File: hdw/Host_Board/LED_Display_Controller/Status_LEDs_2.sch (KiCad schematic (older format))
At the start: 16 parts

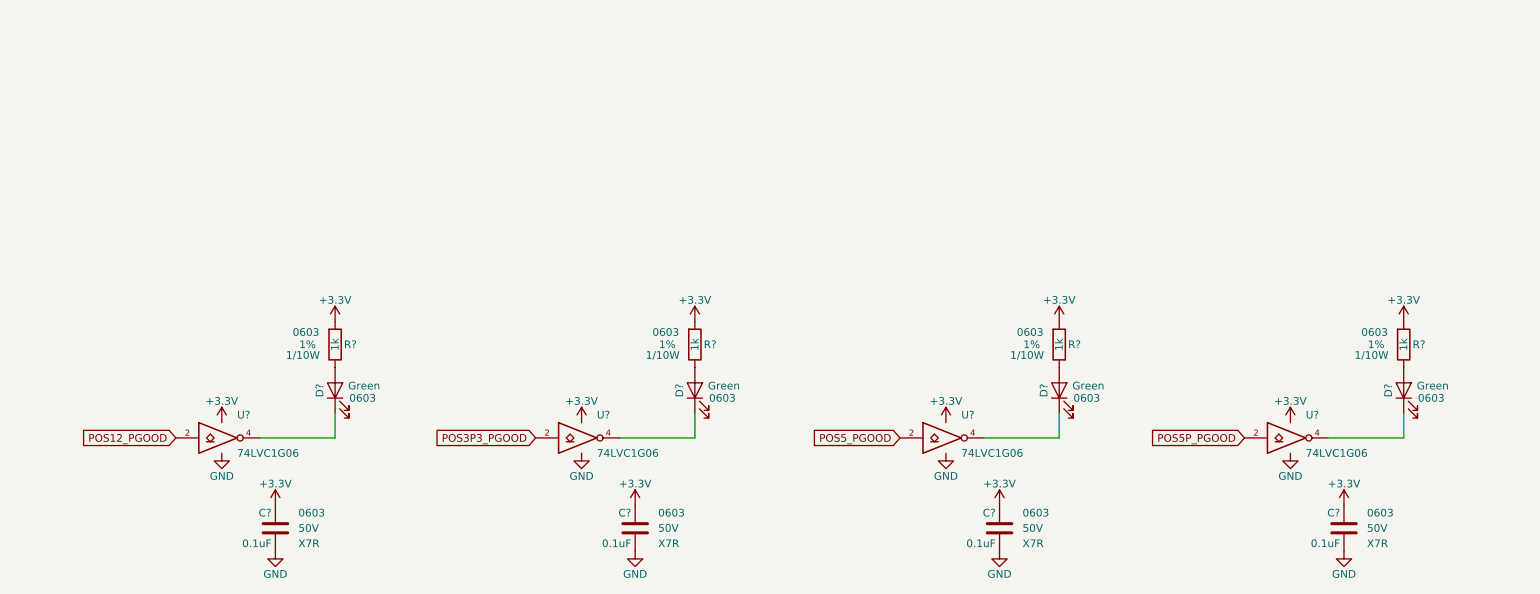
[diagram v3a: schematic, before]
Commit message: Added titles and MU logo to each sheet
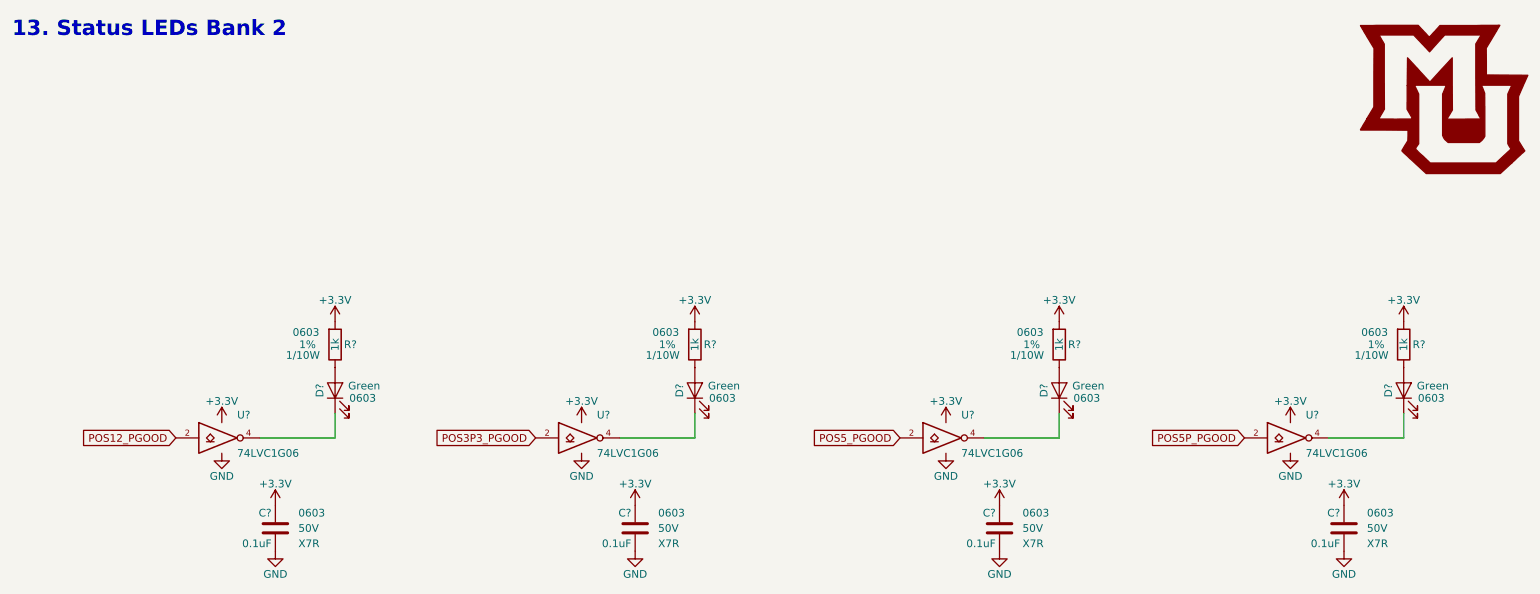
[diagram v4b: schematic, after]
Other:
- note added: "13. Status LEDs Bank 2"
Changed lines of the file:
@@
 AR Path="/5BB844FD/5BF380D7" Ref="#PWR?"  Part="1"
 AR Path="/5BF346B3/5BF380D7" Ref="#PWR0546"  Part="1"
-F 0 "#PWR?" H 2660 2400 50  0001 C CNN
+F 0 "#PWR0546" H 2660 2400 50  0001 C CNN
 F 1 "+3.3V" H 2660 2690 50  0000 C CNN
 F 2 "" H 2660 2550 50  0001 C CNN
@@
 AR Path="/5BB844FD/5BF380E5" Ref="#PWR?"  Part="1"
 AR Path="/5BF346B3/5BF380E5" Ref="#PWR0547"  Part="1"
-F 0 "#PWR?" H 1920 3160 50  0001 C CNN
+F 0 "#PWR0547" H 1920 3160 50  0001 C CNN
 F 1 "GND" H 1920 3260 50  0000 C CNN
 F 2 "" H 1920 3410 50  0001 C CNN
@@
 AR Path="/5BB844FD/5BF380EB" Ref="#PWR?"  Part="1"
 AR Path="/5BF346B3/5BF380EB" Ref="#PWR0548"  Part="1"
-F 0 "#PWR?" H 1920 3060 50  0001 C CNN
+F 0 "#PWR0548" H 1920 3060 50  0001 C CNN
 F 1 "+3.3V" H 1920 3350 50  0000 C CNN
 F 2 "" H 1920 3210 50  0001 C CNN
@@
 AR Path="/5BB844FD/5BF380FE" Ref="#PWR?"  Part="1"
 AR Path="/5BF346B3/5BF380FE" Ref="#PWR0549"  Part="1"
-F 0 "#PWR?" H 2270 3800 50  0001 C CNN
+F 0 "#PWR0549" H 2270 3800 50  0001 C CNN
 F 1 "GND" H 2270 3900 50  0000 C CNN
 F 2 "" H 2270 4050 50  0001 C CNN
@@
 AR Path="/5BB844FD/5BF38104" Ref="#PWR?"  Part="1"
 AR Path="/5BF346B3/5BF38104" Ref="#PWR0550"  Part="1"
-F 0 "#PWR?" H 2270 3600 50  0001 C CNN
+F 0 "#PWR0550" H 2270 3600 50  0001 C CNN
 F 1 "+3.3V" H 2270 3890 50  0000 C CNN
 F 2 "" H 2270 3750 50  0001 C CNN
@@
 AR Path="/5BB844FD/5BF39F2A" Ref="#PWR?"  Part="1"
 AR Path="/5BF346B3/5BF39F2A" Ref="#PWR0551"  Part="1"
-F 0 "#PWR?" H 5010 2400 50  0001 C CNN
+F 0 "#PWR0551" H 5010 2400 50  0001 C CNN
 F 1 "+3.3V" H 5010 2690 50  0000 C CNN
 F 2 "" H 5010 2550 50  0001 C CNN
@@
 AR Path="/5BB844FD/5BF39F38" Ref="#PWR?"  Part="1"
 AR Path="/5BF346B3/5BF39F38" Ref="#PWR0552"  Part="1"
-F 0 "#PWR?" H 4270 3160 50  0001 C CNN
+F 0 "#PWR0552" H 4270 3160 50  0001 C CNN
 F 1 "GND" H 4270 3260 50  0000 C CNN
 F 2 "" H 4270 3410 50  0001 C CNN
@@
 AR Path="/5BB844FD/5BF39F3E" Ref="#PWR?"  Part="1"
 AR Path="/5BF346B3/5BF39F3E" Ref="#PWR0553"  Part="1"
-F 0 "#PWR?" H 4270 3060 50  0001 C CNN
+F 0 "#PWR0553" H 4270 3060 50  0001 C CNN
 F 1 "+3.3V" H 4270 3350 50  0000 C CNN
 F 2 "" H 4270 3210 50  0001 C CNN
@@
 AR Path="/5BB844FD/5BF39F51" Ref="#PWR?"  Part="1"
 AR Path="/5BF346B3/5BF39F51" Ref="#PWR0554"  Part="1"
-F 0 "#PWR?" H 4620 3800 50  0001 C CNN
+F 0 "#PWR0554" H 4620 3800 50  0001 C CNN
 F 1 "GND" H 4620 3900 50  0000 C CNN
 F 2 "" H 4620 4050 50  0001 C CNN
@@
 AR Path="/5BB844FD/5BF39F57" Ref="#PWR?"  Part="1"
 AR Path="/5BF346B3/5BF39F57" Ref="#PWR0555"  Part="1"
-F 0 "#PWR?" H 4620 3600 50  0001 C CNN
+F 0 "#PWR0555" H 4620 3600 50  0001 C CNN
 F 1 "+3.3V" H 4620 3890 50  0000 C CNN
 F 2 "" H 4620 3750 50  0001 C CNN
@@
 AR Path="/5BB844FD/5BF3BDB4" Ref="#PWR?"  Part="1"
 AR Path="/5BF346B3/5BF3BDB4" Ref="#PWR0556"  Part="1"
-F 0 "#PWR?" H 7390 2400 50  0001 C CNN
+F 0 "#PWR0556" H 7390 2400 50  0001 C CNN
 F 1 "+3.3V" H 7390 2690 50  0000 C CNN
 F 2 "" H 7390 2550 50  0001 C CNN
@@
 AR Path="/5BB844FD/5BF3BDC2" Ref="#PWR?"  Part="1"
 AR Path="/5BF346B3/5BF3BDC2" Ref="#PWR0557"  Part="1"
-F 0 "#PWR?" H 6650 3160 50  0001 C CNN
+F 0 "#PWR0557" H 6650 3160 50  0001 C CNN
 F 1 "GND" H 6650 3260 50  0000 C CNN
 F 2 "" H 6650 3410 50  0001 C CNN
@@
 AR Path="/5BB844FD/5BF3BDC8" Ref="#PWR?"  Part="1"
 AR Path="/5BF346B3/5BF3BDC8" Ref="#PWR0558"  Part="1"
-F 0 "#PWR?" H 6650 3060 50  0001 C CNN
+F 0 "#PWR0558" H 6650 3060 50  0001 C CNN
 F 1 "+3.3V" H 6650 3350 50  0000 C CNN
 F 2 "" H 6650 3210 50  0001 C CNN
@@
 AR Path="/5BB844FD/5BF3BDDB" Ref="#PWR?"  Part="1"
 AR Path="/5BF346B3/5BF3BDDB" Ref="#PWR0559"  Part="1"
-F 0 "#PWR?" H 7000 3800 50  0001 C CNN
+F 0 "#PWR0559" H 7000 3800 50  0001 C CNN
 F 1 "GND" H 7000 3900 50  0000 C CNN
 F 2 "" H 7000 4050 50  0001 C CNN
@@
 AR Path="/5BB844FD/5BF3BDE1" Ref="#PWR?"  Part="1"
 AR Path="/5BF346B3/5BF3BDE1" Ref="#PWR0560"  Part="1"
-F 0 "#PWR?" H 7000 3600 50  0001 C CNN
+F 0 "#PWR0560" H 7000 3600 50  0001 C CNN
 F 1 "+3.3V" H 7000 3890 50  0000 C CNN
 F 2 "" H 7000 3750 50  0001 C CNN
@@
 AR Path="/5BB844FD/5BF3DCE4" Ref="#PWR?"  Part="1"
 AR Path="/5BF346B3/5BF3DCE4" Ref="#PWR0561"  Part="1"
-F 0 "#PWR?" H 9640 2400 50  0001 C CNN
+F 0 "#PWR0561" H 9640 2400 50  0001 C CNN
 F 1 "+3.3V" H 9640 2690 50  0000 C CNN
 F 2 "" H 9640 2550 50  0001 C CNN
@@
 AR Path="/5BB844FD/5BF3DCF2" Ref="#PWR?"  Part="1"
 AR Path="/5BF346B3/5BF3DCF2" Ref="#PWR0562"  Part="1"
-F 0 "#PWR?" H 8900 3160 50  0001 C CNN
+F 0 "#PWR0562" H 8900 3160 50  0001 C CNN
 F 1 "GND" H 8900 3260 50  0000 C CNN
 F 2 "" H 8900 3410 50  0001 C CNN
@@
 AR Path="/5BB844FD/5BF3DCF8" Ref="#PWR?"  Part="1"
 AR Path="/5BF346B3/5BF3DCF8" Ref="#PWR0563"  Part="1"
-F 0 "#PWR?" H 8900 3060 50  0001 C CNN
+F 0 "#PWR0563" H 8900 3060 50  0001 C CNN
 F 1 "+3.3V" H 8900 3350 50  0000 C CNN
 F 2 "" H 8900 3210 50  0001 C CNN
@@
 AR Path="/5BB844FD/5BF3DD0B" Ref="#PWR?"  Part="1"
 AR Path="/5BF346B3/5BF3DD0B" Ref="#PWR0564"  Part="1"
-F 0 "#PWR?" H 9250 3800 50  0001 C CNN
+F 0 "#PWR0564" H 9250 3800 50  0001 C CNN
 F 1 "GND" H 9250 3900 50  0000 C CNN
 F 2 "" H 9250 4050 50  0001 C CNN
@@
 AR Path="/5BB844FD/5BF3DD11" Ref="#PWR?"  Part="1"
 AR Path="/5BF346B3/5BF3DD11" Ref="#PWR0565"  Part="1"
-F 0 "#PWR?" H 9250 3600 50  0001 C CNN
+F 0 "#PWR0565" H 9250 3600 50  0001 C CNN
 F 1 "+3.3V" H 9250 3890 50  0000 C CNN
 F 2 "" H 9250 3750 50  0001 C CNN
@@
 Text GLabel 8600 3310 0    50   Input ~ 0
 POS5P_PGOOD
+Text Notes 550  700  0    100  ~ 20
+13. Status LEDs Bank 2
+$Comp
+L LED_Display_Local_Library:MU_Logo #G?
+U 1 1 5BFF7ABF
+P 9900 1100
+F 0 "#G?" H 9900 614 60  0001 C CNN
+F 1 "MU_Logo" H 9900 1586 60  0001 C CNN
+F 2 "" H 9900 1100 50  0001 C CNN
+F 3 "" H 9900 1100 50  0001 C CNN
+	1    9900 1100
+	1    0    0    -1
+$EndComp
 $EndSCHEMATC
